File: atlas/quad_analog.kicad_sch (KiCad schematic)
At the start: 28 parts, among them U701 MCP6004, U702 SRV05-4, U703 NC7SB3157P6X, U704 NC7SB3157P6X

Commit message: pin mapping
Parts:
- renumbered C701 to C901, C702 to C902, C703 to C903, C704 to C904, C705 to C905, R701 to R901, R702 to R902, R703 to R903, R704 to R904, R705 to R905, R706 to R906, R707 to R907, R708 to R908, R709 to R909, R710 to R910, R711 to R911, R712 to R912, RN701 to RN901, U701 to U901, U702 to U902, U703 to U903, U704 to U904

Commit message: progress
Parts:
- renumbered C901 to C1601, C902 to C1602, C903 to C1603, C904 to C1604, C905 to C1605, R901 to R1601, R902 to R1602, R903 to R1603, R904 to R1604, R905 to R1605, R906 to R1606, R907 to R1607, R908 to R1608, R909 to R1609, R910 to R1610, R911 to R1611, R912 to R1612, RN901 to RN1601, U901 to U1601, U902 to U1602, U903 to U1603, U904 to U1604

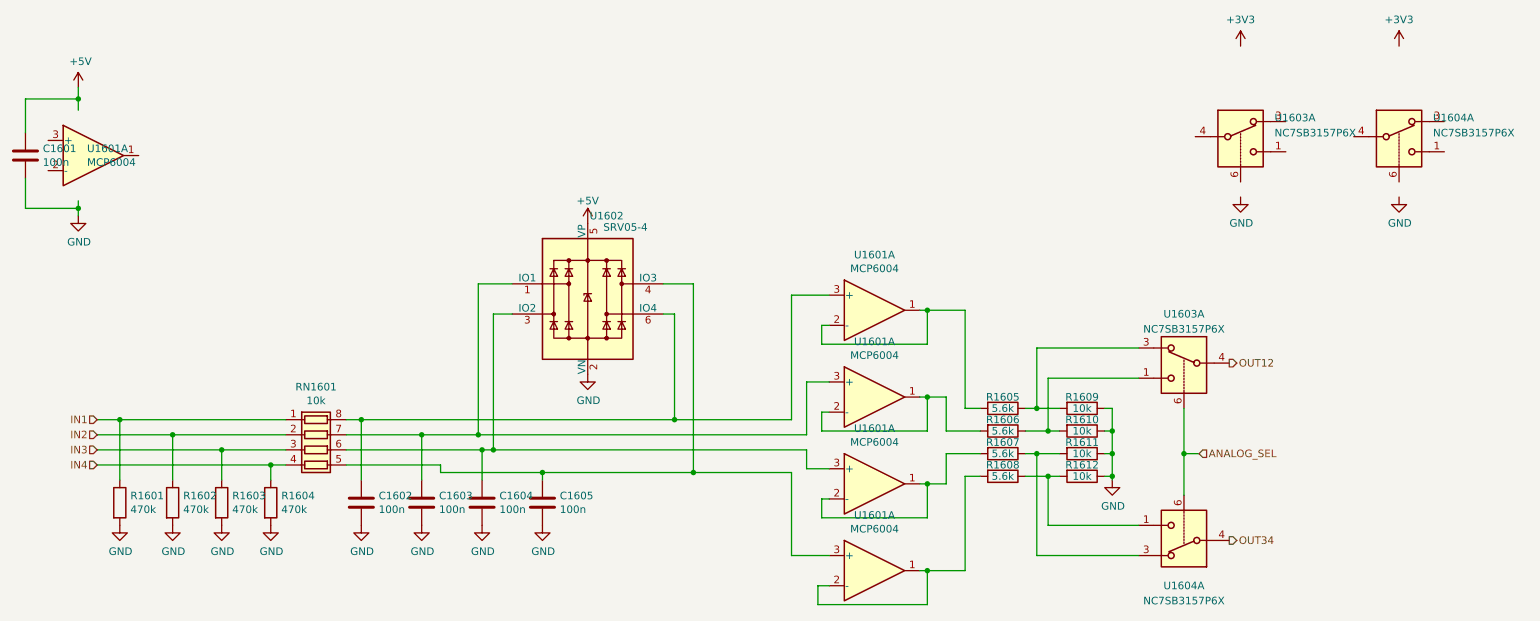
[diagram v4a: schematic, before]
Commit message: footprints & lcsc
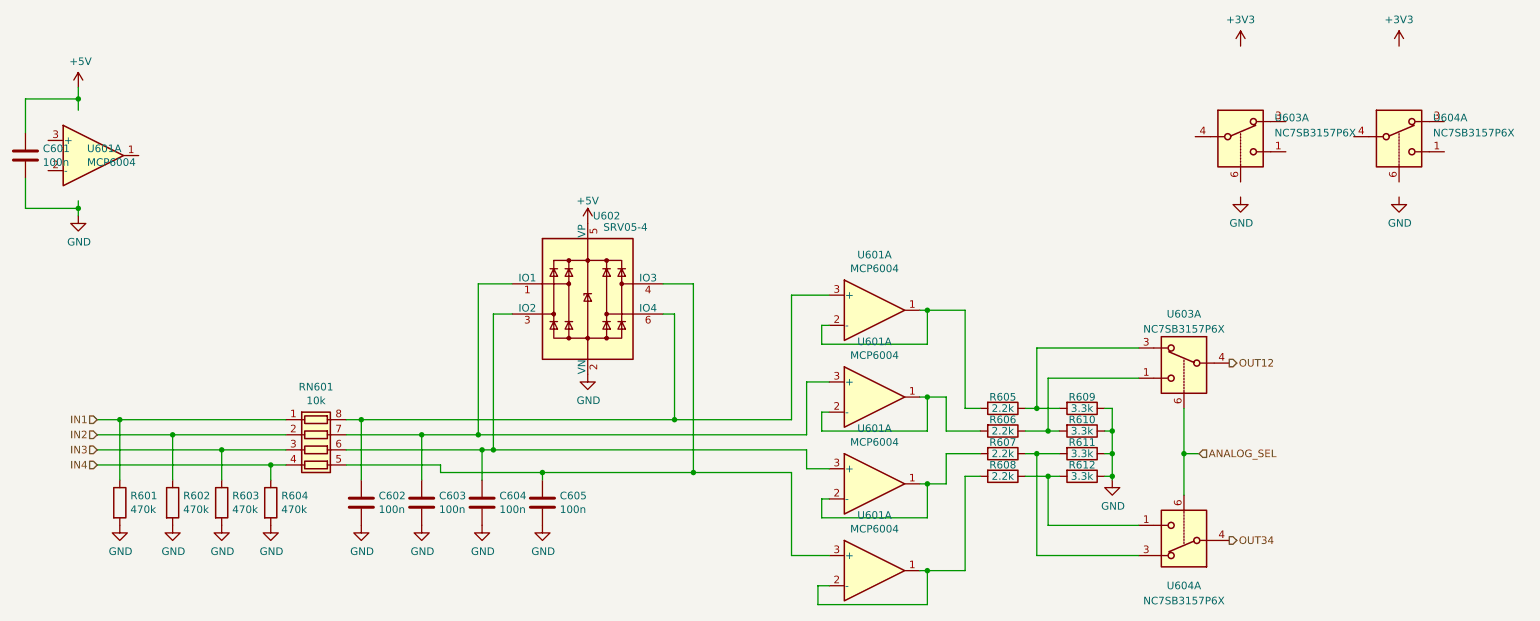
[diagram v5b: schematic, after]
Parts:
- C601: renamed from C1601; footprint Capacitor_SMD:C_0603_1608Metric -> Capacitor_SMD:C_0402_1005Metric; LCSC C14663 -> C1525
- R605: renamed from R1605; value 5.6k -> 2.2k; LCSC C25908 -> C25879
- R606: renamed from R1606; value 5.6k -> 2.2k; LCSC C25908 -> C25879
- R607: renamed from R1607; value 5.6k -> 2.2k; LCSC C25908 -> C25879
- R608: renamed from R1608; value 5.6k -> 2.2k; LCSC C25908 -> C25879
- R609: renamed from R1609; value 10k -> 3.3k; LCSC C25744 -> C25890
- R610: renamed from R1610; value 10k -> 3.3k; LCSC C25744 -> C25890
- R611: renamed from R1611; value 10k -> 3.3k; LCSC C25744 -> C25890
- R612: renamed from R1612; value 10k -> 3.3k; LCSC C25744 -> C25890
- renumbered C1602 to C602, C1603 to C603, C1604 to C604, C1605 to C605, R1601 to R601, R1602 to R602, R1603 to R603, R1604 to R604, RN1601 to RN601, U1601 to U601, U1602 to U602, U1603 to U603, U1604 to U604

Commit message: upgrade kicad
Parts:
- renumbered C601 to C501, C602 to C502, C603 to C503, C604 to C504, C605 to C505, R601 to R501, R602 to R502, R603 to R503, R604 to R504, R605 to R505, R606 to R506, R607 to R507, R608 to R508, R609 to R509, R610 to R510, R611 to R511, R612 to R512, RN601 to RN501, U601 to U501, U602 to U502, U603 to U503, U604 to U504
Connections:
- net +3V3: now also U503.5 (V+), U504.5 (V+)
- net +5V: now also U501.4 (V+)
- net GND: now also U501.11 (V-), U503.2 (GND), U504.2 (GND)
- net at C503.1, RN501.7 (R2.2), U502.1 (IO1): now also U501.5 (+); no longer U501.3 (+)
- net at C504.1, RN501.6 (R3.2), U502.3 (IO2): now also U501.10 (+); no longer U501.3 (+)
- net at C505.1, RN501.5 (R4.2), U502.4 (IO3): now also U501.12 (+); no longer U501.3 (+)
- new net: R506.2, U501.6 (-), U501.7
- new net: R507.2, U501.8, U501.9 (-)
- new net: R508.2, U501.13 (-), U501.14
